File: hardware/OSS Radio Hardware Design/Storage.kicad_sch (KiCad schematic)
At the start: 7 parts, among them J4 MEM2061-01-188-00-A_REVA, U5 MX25L25645GM2I-08G

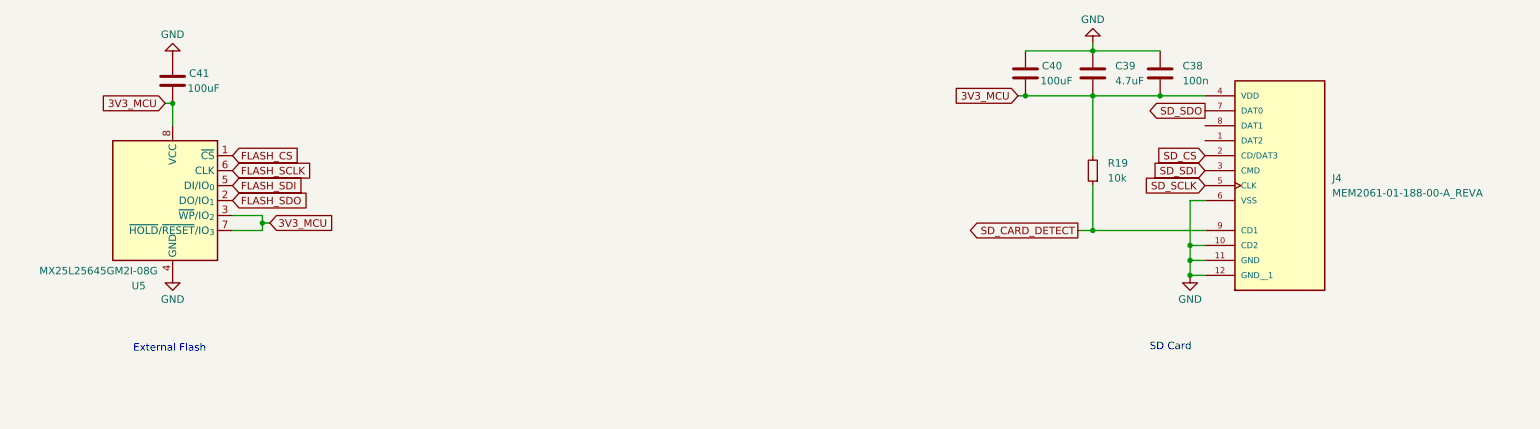
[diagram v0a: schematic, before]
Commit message: finished schematic for audio
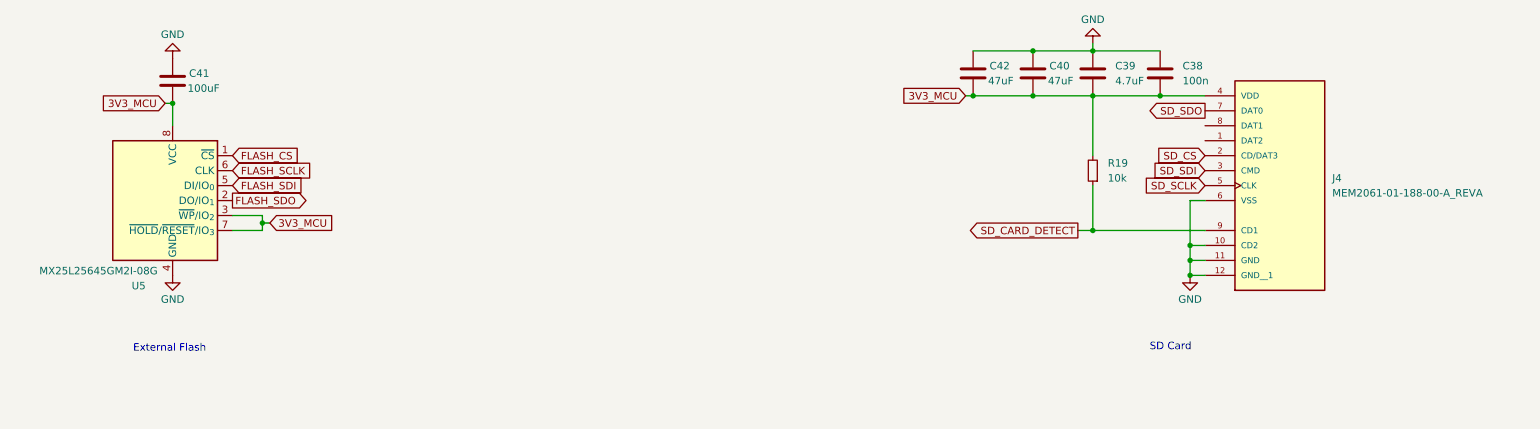
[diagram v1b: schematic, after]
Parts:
- added C42: 47uF, symbol Device:C
- C40: value 100uF -> 47uF
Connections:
- net 3V3_MCU: now also C42.2
- net GND: now also C42.1
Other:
- moved on the sheet: C40
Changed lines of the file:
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@@
+	)
+	(junction
+		(at 186.69 39.37)
+		(diameter 0)
+		(color 0 0 0 0)
+	)
+	(junction
+		(at 196.85 31.75)
+		(diameter 0)
+		(color 0 0 0 0)
 	)
 	(junction
@@
 	)
 	(junction
-		(at 195.58 39.37)
-		(diameter 0)
-		(color 0 0 0 0)
-	)
-	(junction
 		(at 207.01 62.23)
 		(diameter 0)
@@
 	)
 	(junction
+		(at 196.85 39.37)
+		(diameter 0)
+		(color 0 0 0 0)
+	)
+	(junction
 		(at 50.8 40.64)
 		(diameter 0)
@@
 	(wire
 		(pts
+			(xy 186.69 39.37) (xy 185.42 39.37)
+		)
+		(stroke
+			(width 0)
+			(type default)
+		)
+	)
+	(wire
+		(pts
 			(xy 207.01 30.48) (xy 207.01 31.75)
 		)
@@
 	(wire
 		(pts
+			(xy 196.85 39.37) (xy 207.01 39.37)
+		)
+		(stroke
+			(width 0)
+			(type default)
+		)
+	)
+	(wire
+		(pts
 			(xy 204.47 62.23) (xy 207.01 62.23)
 		)
@@
 	(wire
 		(pts
-			(xy 194.31 39.37) (xy 195.58 39.37)
-		)
-		(stroke
-			(width 0)
-			(type default)
-		)
-	)
-	(wire
-		(pts
 			(xy 207.01 31.75) (xy 218.44 31.75)
 		)
@@
 	(wire
 		(pts
-			(xy 195.58 39.37) (xy 207.01 39.37)
+			(xy 186.69 31.75) (xy 196.85 31.75)
+		)
+		(stroke
+			(width 0)
+			(type default)
+		)
+	)
+	(wire
+		(pts
+			(xy 186.69 39.37) (xy 196.85 39.37)
+		)
+		(stroke
+			(width 0)
+			(type default)
+		)
+	)
+	(wire
+		(pts
+			(xy 196.85 31.75) (xy 207.01 31.75)
 		)
 		(stroke
@@
 		(pts
 			(xy 218.44 39.37) (xy 226.06 39.37)
-		)
-		(stroke
-			(width 0)
-			(type default)
-		)
-	)
-	(wire
-		(pts
-			(xy 195.58 31.75) (xy 207.01 31.75)
 		)
 		(stroke
@@
 	)
 	(global_label "FLASH_SDO"
-		(shape input)
+		(shape output)
 		(at 60.96 57.15 0)
 		(fields_autoplaced yes)
@@
 	(global_label "3V3_MCU"
 		(shape input)
-		(at 194.31 39.37 180)
+		(at 185.42 39.37 180)
 		(fields_autoplaced yes)
 		(effects
@@
 		)
 		(property "Intersheetrefs" "${INTERSHEET_REFS}"
-			(at 182.7977 39.37 0)
+			(at 173.9077 39.37 0)
 			(effects
 				(font
@@
 	(symbol
 		(lib_id "Device:C")
-		(at 195.58 35.56 0)
+		(at 196.85 35.56 0)
 		(unit 1)
 		(exclude_from_sim no)
@@
 		(dnp no)
 		(property "Reference" "C40"
-			(at 198.374 34.29 0)
-			(effects
-				(font
-					(size 1.27 1.27)
-				)
-				(justify left)
-			)
-		)
-		(property "Value" "100uF"
-			(at 198.12 36.83 0)
+			(at 199.644 34.29 0)
+			(effects
+				(font
+					(size 1.27 1.27)
+				)
+				(justify left)
+			)
+		)
+		(property "Value" "47uF"
+			(at 199.39 36.83 0)
 			(effects
 				(font
@@
 		)
 		(property "Footprint" ""
-			(at 196.5452 39.37 0)
+			(at 197.8152 39.37 0)
 			(effects
 				(font
@@
 		)
 		(property "Datasheet" "~"
-			(at 195.58 35.56 0)
+			(at 196.85 35.56 0)
 			(effects
 				(font
@@
 		)
 		(property "Description" "Unpolarized capacitor"
-			(at 195.58 35.56 0)
+			(at 196.85 35.56 0)
 			(effects
 				(font
@@
 					(unit 1)
 				)
+			)
+		)
+	)
+	(symbol
+		(lib_id "Device:C")
+		(at 186.69 35.56 0)
+		(unit 1)
+		(exclude_from_sim no)
+		(in_bom yes)
+		(on_board yes)
+		(dnp no)
+		(property "Reference" "C42"
+			(at 189.484 34.29 0)
+			(effects
+				(font
+					(size 1.27 1.27)
+				)
+				(justify left)
+			)
+		)
+		(property "Value" "47uF"
+			(at 189.23 36.83 0)
+			(effects
+				(font
+					(size 1.27 1.27)
+				)
+				(justify left)
+			)
+		)
+		(property "Footprint" ""
+			(at 187.6552 39.37 0)
+			(effects
+				(font
+					(size 1.27 1.27)
+				)
+				(hide yes)
+			)
+		)
+		(property "Datasheet" "~"
+			(at 186.69 35.56 0)
+			(effects
+				(font
+					(size 1.27 1.27)
+				)
+				(hide yes)
+			)
+		)
+		(property "Description" "Unpolarized capacitor"
+			(at 186.69 35.56 0)
+			(effects
+				(font
+					(size 1.27 1.27)
+				)
+				(hide yes)
+			)
+		)
+		(pin "1"
+		)
+		(pin "2"
+		)
+		(instances
+			(project "OSS Radio Hardware Design"
+				(path "/fd5c68a7-f5d0-4135-a258-bde3ebf63307/f2573a87-f70c-4caf-8131-0e6b13f03101"
+					(reference "C42")
+					(unit 1)
+				)

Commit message: BOM consolidation
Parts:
- C39: value 4.7uF -> 4.7u
- C40, C42: value 47uF -> 47u
- C41: value 100uF -> 100n
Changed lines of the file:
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@@
 			)
 		)
-		(property "Value" "47uF"
+		(property "Value" "47u"
 			(at 199.39 36.83 0)
 			(effects
@@
 			)
 		)
-		(property "Value" "4.7uF"
+		(property "Value" "4.7u"
 			(at 210.82 36.8299 0)
 			(effects
@@
 			)
 		)
-		(property "Value" "100uF"
+		(property "Value" "100n"
 			(at 53.34 38.1 0)
 			(effects
@@
 			)
 		)
-		(property "Value" "47uF"
+		(property "Value" "47u"
 			(at 189.23 36.83 0)
 			(effects

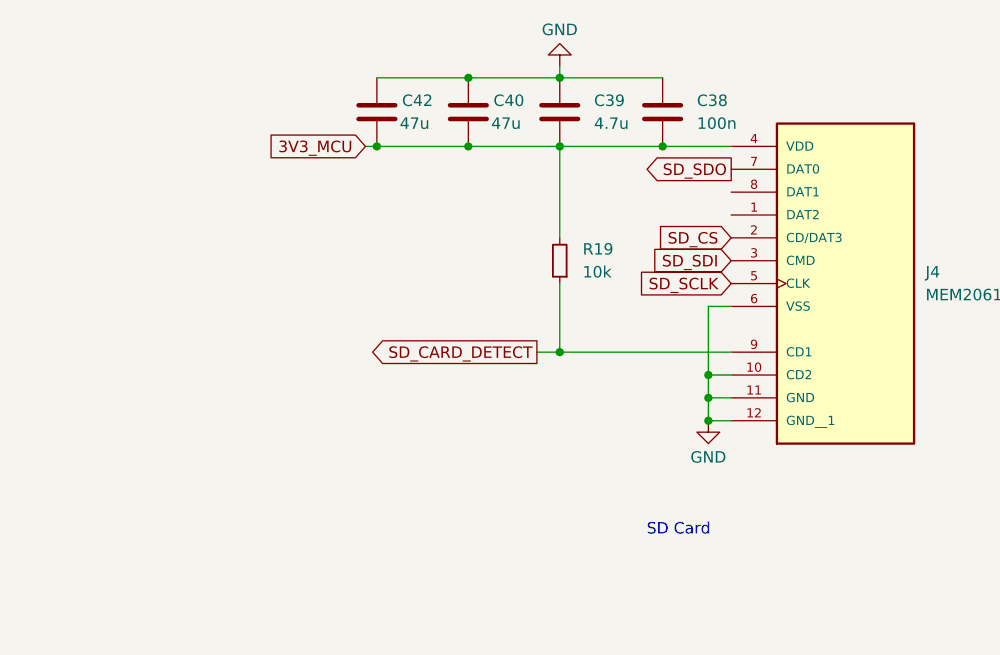
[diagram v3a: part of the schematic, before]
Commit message: added ESD diodes, MARS resistor, Charge LED, Status LED
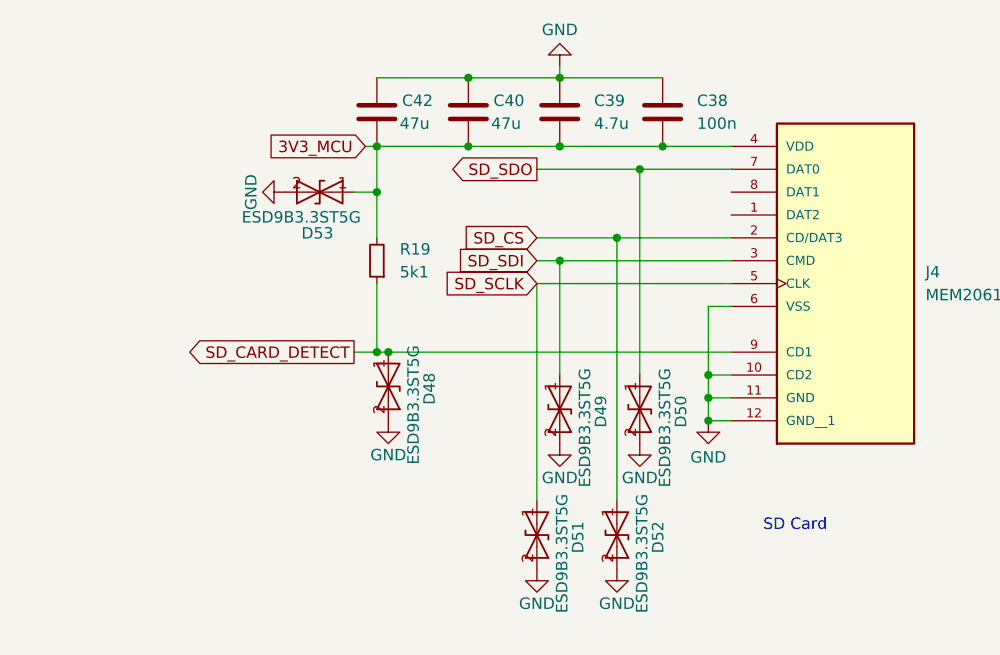
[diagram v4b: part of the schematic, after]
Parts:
- added D48, D49, D50, D51, D52, D53: ESD9B3.3ST5G, Diode_SMD:D_SOD-923, symbol Diode:ESD9B3.3ST5G
- R19: value 10k -> 5k1
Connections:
- net 3V3_MCU: now also D53.1 (A1)
- net GND: now also D48.2 (A2), D49.2 (A2), D50.2 (A2), D51.2 (A2), D52.2 (A2), D53.2 (A2)
- net SD_CARD_DETECT: now also D48.1 (A1)
- net SD_CS: now also D52.1 (A1)
- net SD_SCLK: now also D51.1 (A1)
- net SD_SDI: now also D49.1 (A1)
- net SD_SDO: now also D50.1 (A1)
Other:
- moved on the sheet: R19

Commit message: working on fooprints
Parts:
- C38, C41: footprint (none) -> Capacitor_SMD:C_0402_1005Metric_Pad0.74x0.62mm_HandSolder
- C39: footprint (none) -> Capacitor_SMD:C_0603_1608Metric_Pad1.08x0.95mm_HandSolder
- C40, C42: footprint (none) -> Capacitor_SMD:C_1206_3216Metric_Pad1.33x1.80mm_HandSolder
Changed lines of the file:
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@@
 			)
 		)
-		(property "Footprint" ""
+		(property "Footprint" "Capacitor_SMD:C_1206_3216Metric_Pad1.33x1.80mm_HandSolder"
 			(at 197.8152 39.37 0)
 			(effects
@@
 			)
 		)
-		(property "Footprint" ""
+		(property "Footprint" "Capacitor_SMD:C_0603_1608Metric_Pad1.08x0.95mm_HandSolder"
 			(at 207.9752 39.37 0)
 			(effects
@@
 			)
 		)
-		(property "Footprint" ""
+		(property "Footprint" "Capacitor_SMD:C_0402_1005Metric_Pad0.74x0.62mm_HandSolder"
 			(at 51.7652 40.64 0)
 			(effects
@@
 			)
 		)
-		(property "Footprint" ""
+		(property "Footprint" "Capacitor_SMD:C_1206_3216Metric_Pad1.33x1.80mm_HandSolder"
 			(at 187.6552 39.37 0)
 			(effects
@@
 			)
 		)
-		(property "Footprint" ""
+		(property "Footprint" "Capacitor_SMD:C_0402_1005Metric_Pad0.74x0.62mm_HandSolder"
 			(at 219.4052 39.37 0)
 			(effects
